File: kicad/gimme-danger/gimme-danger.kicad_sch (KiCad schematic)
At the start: 45 parts, among them J1 Screw_Terminal_01x04, J2 Barrel_Jack, Q1 AO3400A, Q2 AO3400A, U1 ESP32-S3-WROOM-1, U2 TPD6S300RUKR, U3 U261-241N-4BS2SS, U4 NX20P5090UKAZ, U5 SKRKAEE020, U6 TPS62177DQCR, U7 SKRKAEE020

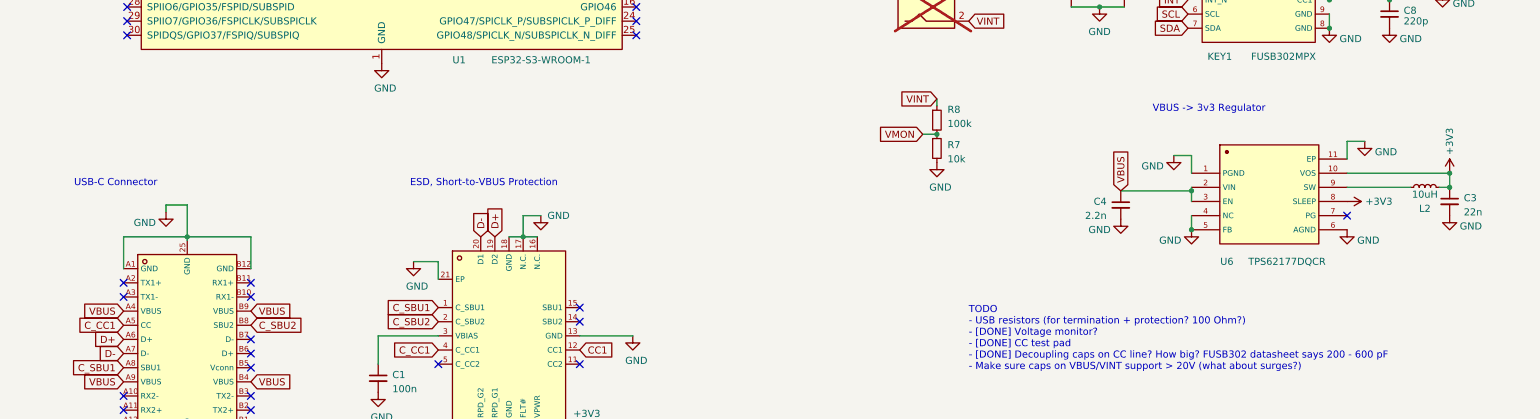
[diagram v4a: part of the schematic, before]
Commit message: Changed to more capable DC-DC converter (up to 1.2A)
Worst case: ESP32-S3 500 mA + FUSB302 500 mA
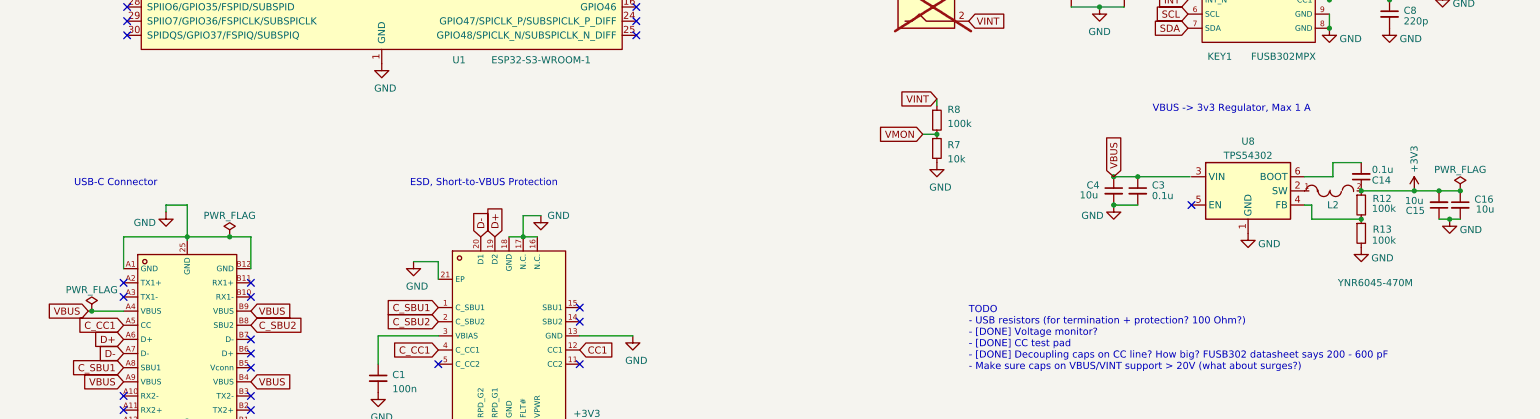
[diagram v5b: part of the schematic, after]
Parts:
- removed L2: 10uH, Inductor_SMD:L_0805_2012Metric, symbol Device:L_Small
- removed U6: TPS62177DQCR, footprint:WSON-10_L3.0-W2.0-P0.50-BL-EP, symbol TPS62177DQCR:TPS62177DQCR
- added C14: 0.1u, Capacitor_SMD:C_0402_1005Metric, symbol Device:C_Small
- added C15, C16: 10u, Capacitor_SMD:C_0603_1608Metric, symbol Device:C_Small
- added L2: YNR6045-470M, footprint:IND-SMD_L6.0-W6.0, symbol YNR6045-470M:YNR6045-470M
- added R12, R13: 100k, Resistor_SMD:R_0402_1005Metric, symbol Device:R_Small
- added U8: TPS54302, Package_TO_SOT_SMD:SOT-23-6, symbol Regulator_Switching:TPS54302
- C3: value 22n -> 0.1u; LCSC C1532 -> C307331
- C4: value 2.2n -> 10u; footprint Capacitor_SMD:C_0402_1005Metric -> Capacitor_SMD:C_0603_1608Metric; LCSC C513667 -> C96446
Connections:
- net +3V3: now also C14.1, C15.2, C16.1, L2.2, R12.1; no longer C3.1
- net GND: now also C15.1, C16.2, R13.2, U8.1 (GND)
- net VBUS: now also C3.1
- new net: R12.2, R13.1, U8.4 (FB)
- new net: L2.1, U8.2 (SW)
- new net: C14.2, U8.6 (BOOT)
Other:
- note added: "VBUS -> 3v3 Regulator, Max 1 A"
- note removed: "VBUS -> 3v3 Regulator"
- moved on the sheet: C4

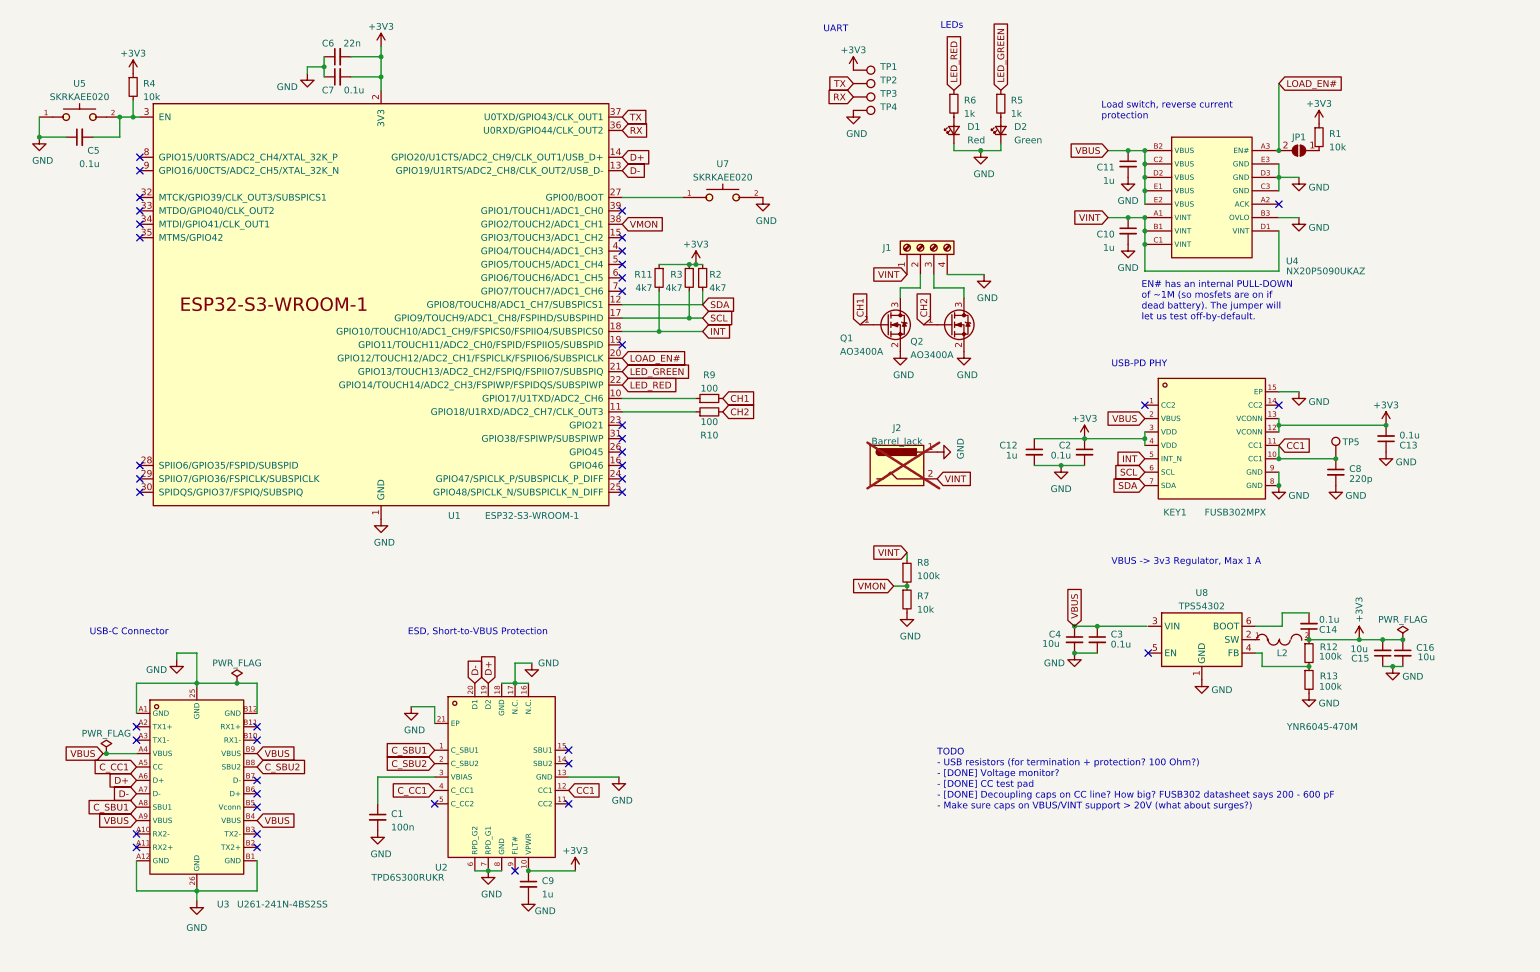
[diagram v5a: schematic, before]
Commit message: Initial partial routing
But I'm not convinced I can route the tiny load switch well. I will
change it back to the same setup as used by luz.
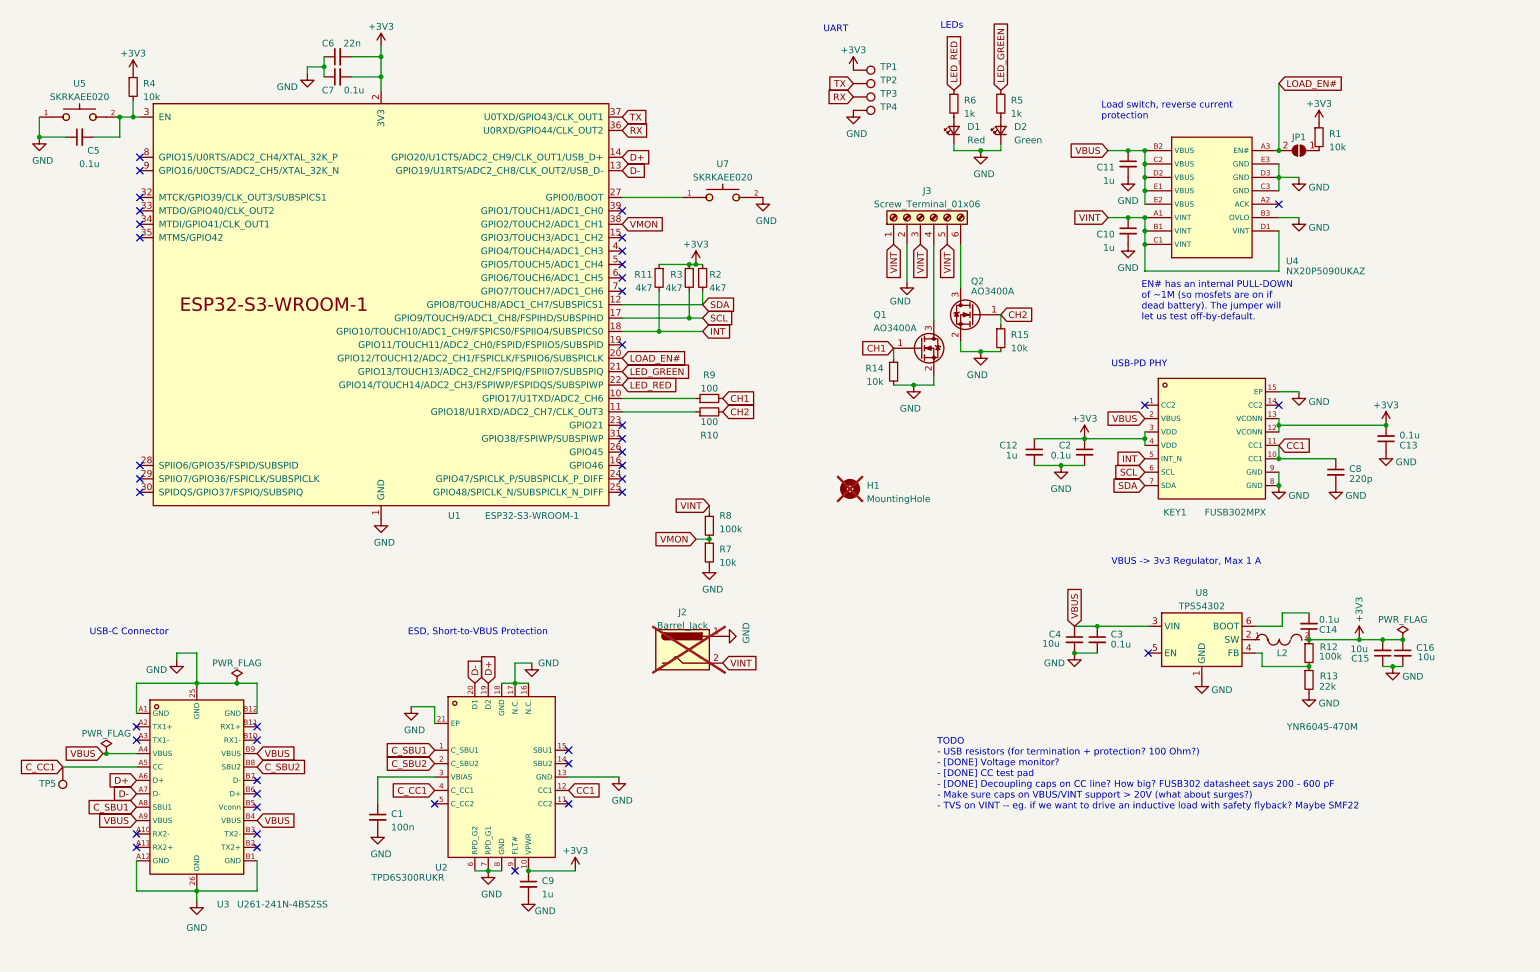
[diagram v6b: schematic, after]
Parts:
- removed J1: Screw_Terminal_01x04, TerminalBlock_Phoenix:TerminalBlock_Phoenix_MKDS-1,5-4_1x04_P5.00mm_Horizontal, symbol Connector:Screw_Terminal_01x04
- added H1: MountingHole, MountingHole:MountingHole_2.2mm_M2_Pad_Via, symbol Mechanical:MountingHole
- added J3: Screw_Terminal_01x06, TerminalBlock_Phoenix:TerminalBlock_Phoenix_MKDS-1,5-6_1x06_P5.00mm_Horizontal, symbol Connector:Screw_Terminal_01x06
- added R14, R15: 10k, Resistor_SMD:R_0402_1005Metric, symbol Device:R_Small
- C1: LCSC C1525 -> C307331
- R13: value 100k -> 22k; LCSC C25741 -> C25768
- TP1, TP2, TP3, TP4, TP5: now left out of the parts list
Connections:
- net CC1: no longer TP5.1
- net CH1: now also R14.1
- net CH2: now also R15.1
- net C_CC1: now also TP5.1
- net GND: now also J3.2 (Pin_2), R14.2, R15.2
- net VBUS: now also U8.3 (VIN)
- net VINT: now also J3.1 (Pin_1), J3.3 (Pin_3), J3.5 (Pin_5)
- net at Q2.3 (D): now also J3.6 (Pin_6)
- net at Q1.3 (D): now also J3.4 (Pin_4)
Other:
- note added: "TODO - USB resistors (for termination + protection? 100 Ohm?) - [DONE] Voltage monitor? - [DONE] CC test pad - [DONE] Decoupling caps on CC line? How big? FUSB302 datasheet says 200 - 600 pF - Make sure caps on VBUS/VINT support > 20V (what about surges?) - TVS on VINT -- eg. if we want to drive an inductive load with safety flyback? Maybe SMF22"
- note removed: "TODO - USB resistors (for termination + protection? 100 Ohm?) - [DONE] Voltage monitor? - [DONE] CC test pad - [DONE] Decoupling caps on CC line? How big? FUSB302 datasheet says 200 - 600 pF - Make sure caps on VBUS/VINT support > 20V (what about surges?)"
- moved on the sheet: J2, Q1, Q2, R7, R8, TP5

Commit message: Schematic with FUSB302 kinda finished
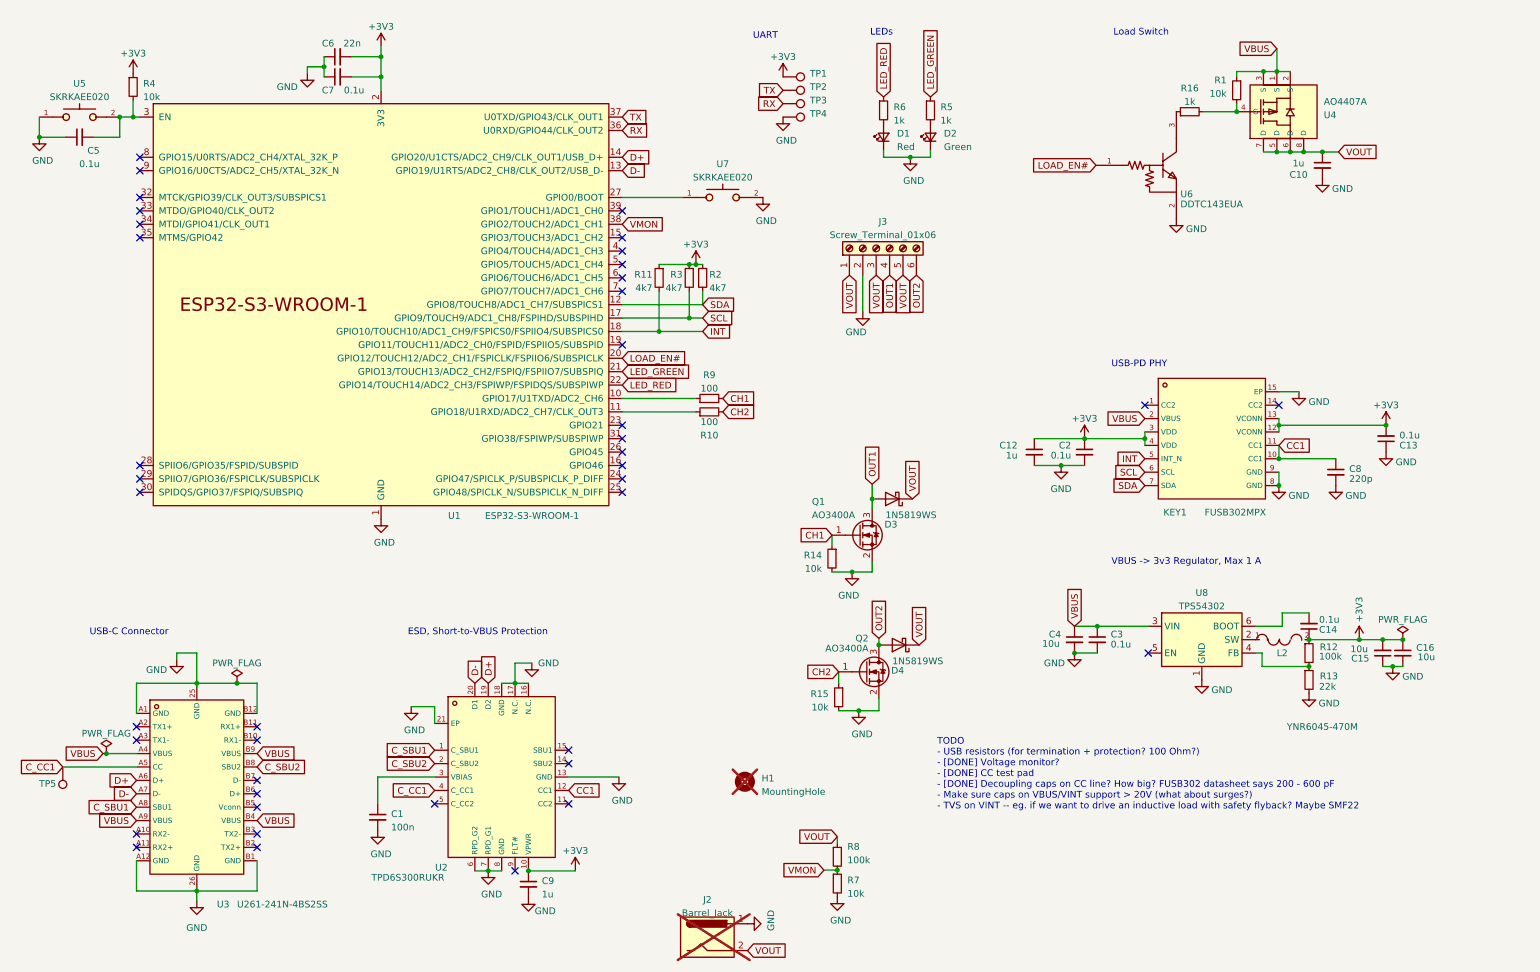
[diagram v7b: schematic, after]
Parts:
- removed C11: 1u, Capacitor_SMD:C_0402_1005Metric, symbol Device:C_Small
- removed JP1: ~, Jumper:SolderJumper-2_P1.3mm_Open_RoundedPad1.0x1.5mm, symbol Jumper:SolderJumper_2_Open
- removed U4: NX20P5090UKAZ, footprint:WLCSP-15_L2.6-W1.6-R3-C5-P0.50-TL_NXP, symbol NX20P5090UKAZ:NX20P5090UKAZ
- added D3, D4: 1N5819WS, Diode_SMD:D_SOD-323, symbol Diode:1N5819WS
- added R16: 1k, Resistor_SMD:R_0402_1005Metric, symbol Device:R_Small
- added U4: AO4407A, footprint:SOIC-8_L4.9-W3.9-P1.27-LS6.0-BL, symbol AO4407A:AO4407A
- added U6: DDTC143EUA, footprint:SOT-323-3_L2.0-W1.3-P1.30-LS2.1-BR, symbol DDTC143EUA-7-F:DDTC143EUA-7-F
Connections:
- net +3V3: no longer R1.1
- net GND: now also U6.2 (GND(0))
- net LOAD_EN#: now also U6.1 (IN)
- net VBUS: now also R1.1, U4.1 (S), U4.2 (S), U4.3 (S)
- net OUT2: now reaches J3.6 (Pin_6), Q2.3 (D)
- net OUT2: now also D4.2 (A)
- net OUT1: now reaches J3.4 (Pin_4), Q1.3 (D)
- net OUT1: now also D3.2 (A)
- net at R1.2: now also R16.2, U4.4 (G)
- net VINT renamed VOUT
- net VOUT: now also D3.1 (K), D4.1 (K), U4.5 (D), U4.6 (D), U4.7 (D), U4.8 (D)
- new net: R16.1, U6.3 (OUT)
- no-connect marks 42 -> 41
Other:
- note added: "Load Switch"
- note removed: "EN# has an internal PULL-DOWN of ~1M (so mosfets are on if dead battery). The jumper will let us test off-by-default."
- note removed: "Load switch, reverse current protection"
- moved on the sheet: C10, D1, D2, H1, J2, J3, Q1, Q2, R14, R15, R5, R6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

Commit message: Better schematic layout
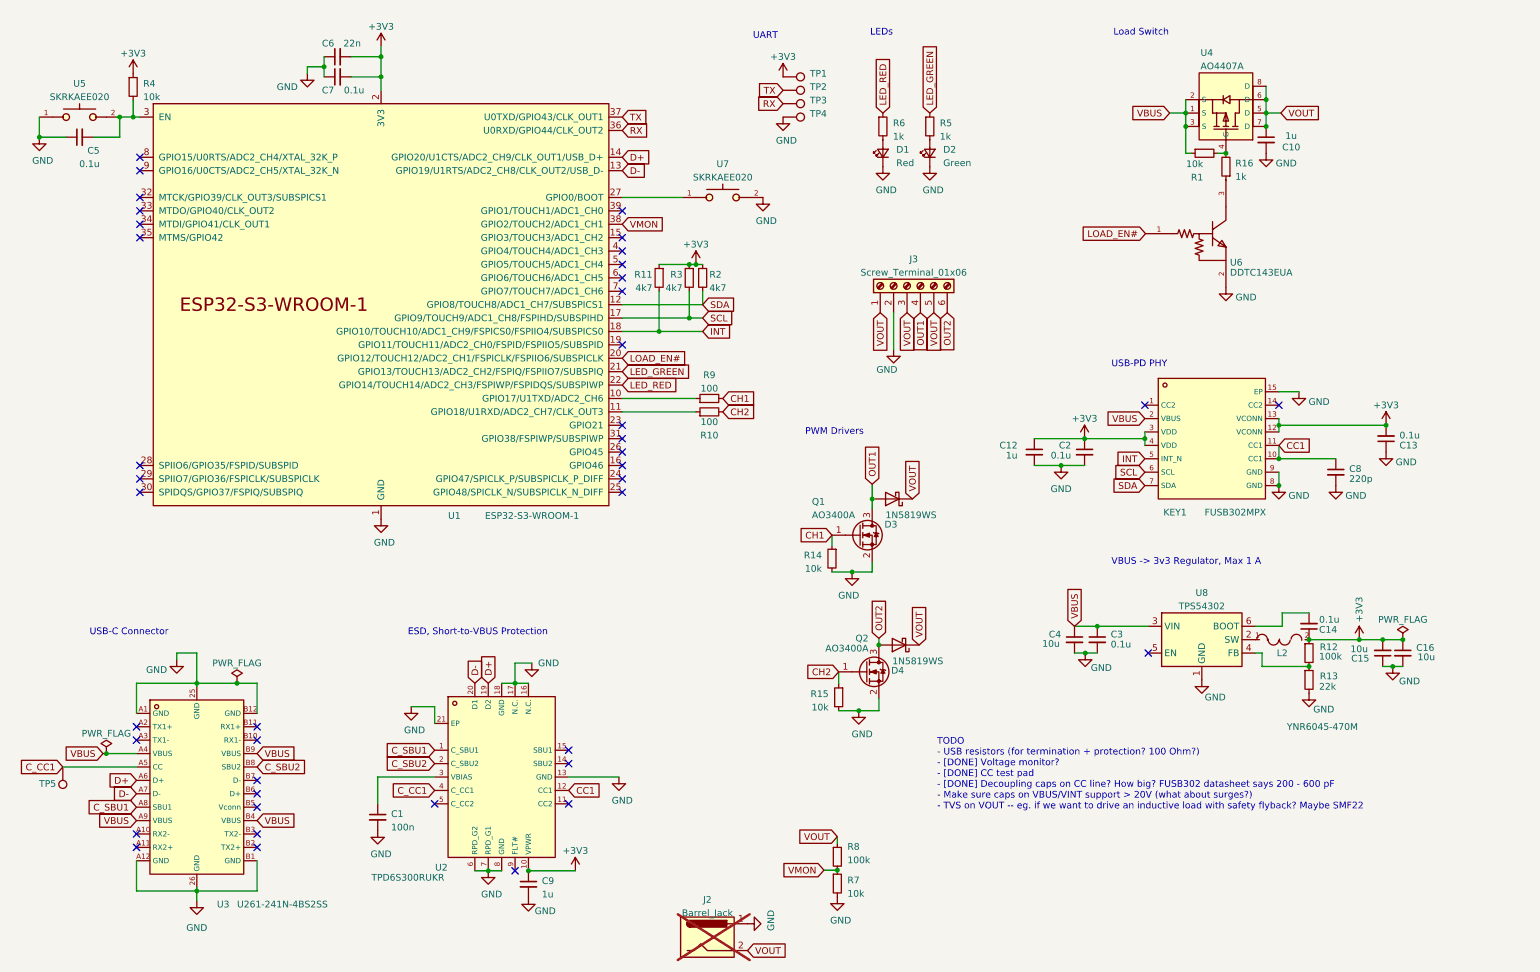
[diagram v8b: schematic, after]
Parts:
- removed H1: MountingHole, MountingHole:MountingHole_2.2mm_M2_Pad_Via, symbol Mechanical:MountingHole
- J3: now left out of the parts list
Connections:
- net VOUT: no longer C10.1, U4.5 (D), U4.6 (D), U4.7 (D), U4.8 (D)
- new net: C10.1, U4.5 (D), U4.6 (D), U4.7 (D), U4.8 (D)
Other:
- note added: "PWM Drivers"
- note added: "TODO - USB resistors (for termination + protection? 100 Ohm?) - [DONE] Voltage monitor? - [DONE] CC test pad - [DONE] Decoupling caps on CC line? How big? FUSB302 datasheet says 200 - 600 pF - Make sure caps on VBUS/VINT support > 20V (what about surges?) - TVS on VOUT -- eg. if we want to drive an inductive load with safety flyback? Maybe SMF22"
- note removed: "TODO - USB resistors (for termination + protection? 100 Ohm?) - [DONE] Voltage monitor? - [DONE] CC test pad - [DONE] Decoupling caps on CC line? How big? FUSB302 datasheet says 200 - 600 pF - Make sure caps on VBUS/VINT support > 20V (what about surges?) - TVS on VINT -- eg. if we want to drive an inductive load with safety flyback? Maybe SMF22"
- moved on the sheet: C10, D1, D2, J3, R1, R16, R5, R6, U4, U6
